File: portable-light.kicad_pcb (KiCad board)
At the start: 4 copper layers, 54.5 x 63.7 mm, 104 parts, among them J1 Prog, J2 Button, J3 Charger, J4 Seven-segment, J5 LOAD, Q1 MMBT2222A, Q2 MMBT2222A, Q3 MMBT2222A, Q4 MMBT2222A, Q5 MMBT2222A, Q6 PHD45N03LTA, Q7 PHD45N03LTA, Q8 MMBT2222A, U1 L78L05_SOT89, U2 ATmega88PA-AU, U3 LTC1733EMSEPBF, Y1 Crystal

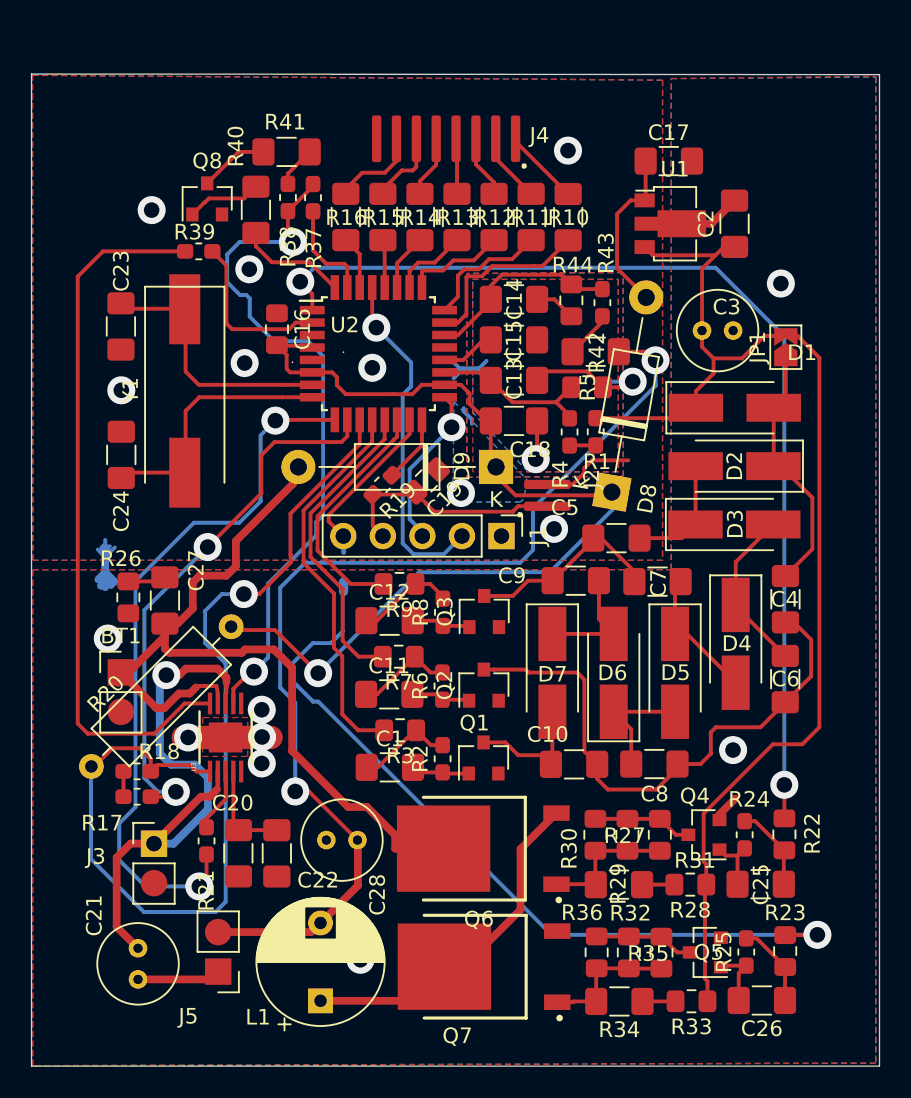
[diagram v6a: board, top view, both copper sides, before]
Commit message: divided schematics into multiple sheets moved to arch
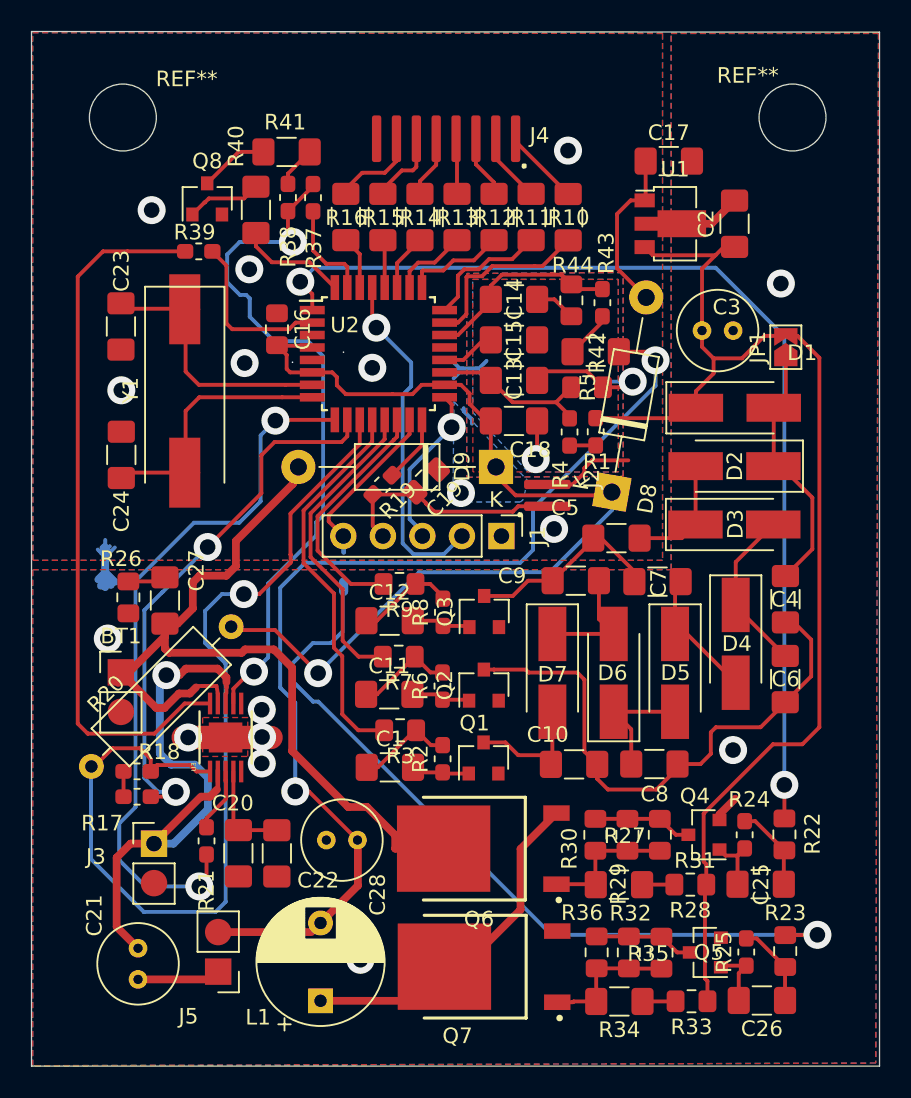
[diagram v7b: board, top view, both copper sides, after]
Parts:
- added REF**: MountingHole_4.3mm_M4, MountingHole:MountingHole_4.3mm_M4, F.Cu at (171.1, 71.0)
- added REF**: MountingHole_4.3mm_M4, MountingHole:MountingHole_4.3mm_M4, F.Cu at (128.1, 71.0)
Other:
- board size 54.5 x 63.7 mm -> 54.5 x 66.5 mm

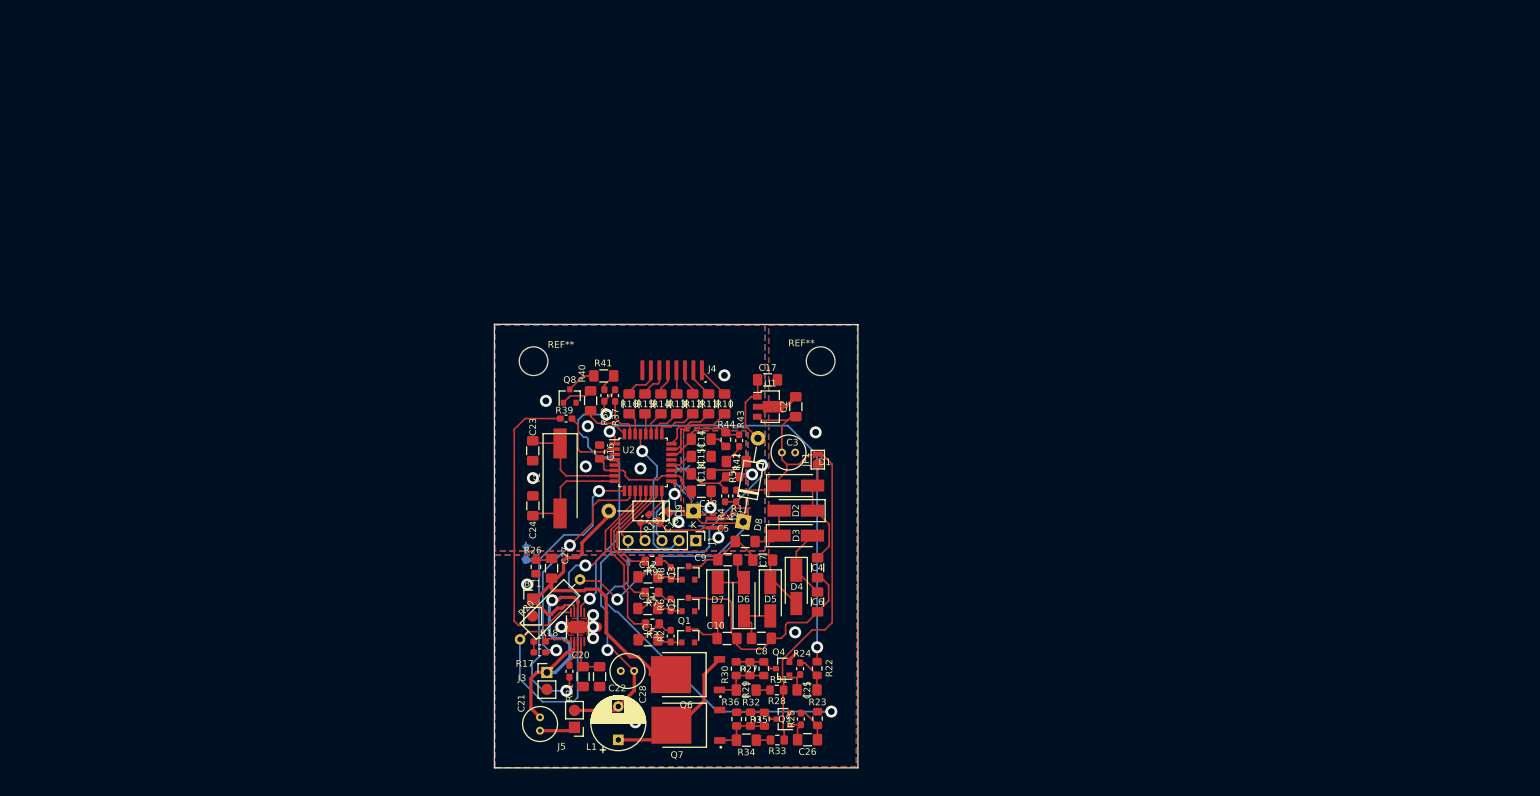
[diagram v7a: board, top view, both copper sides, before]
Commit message: Schematics redesigned and fixed
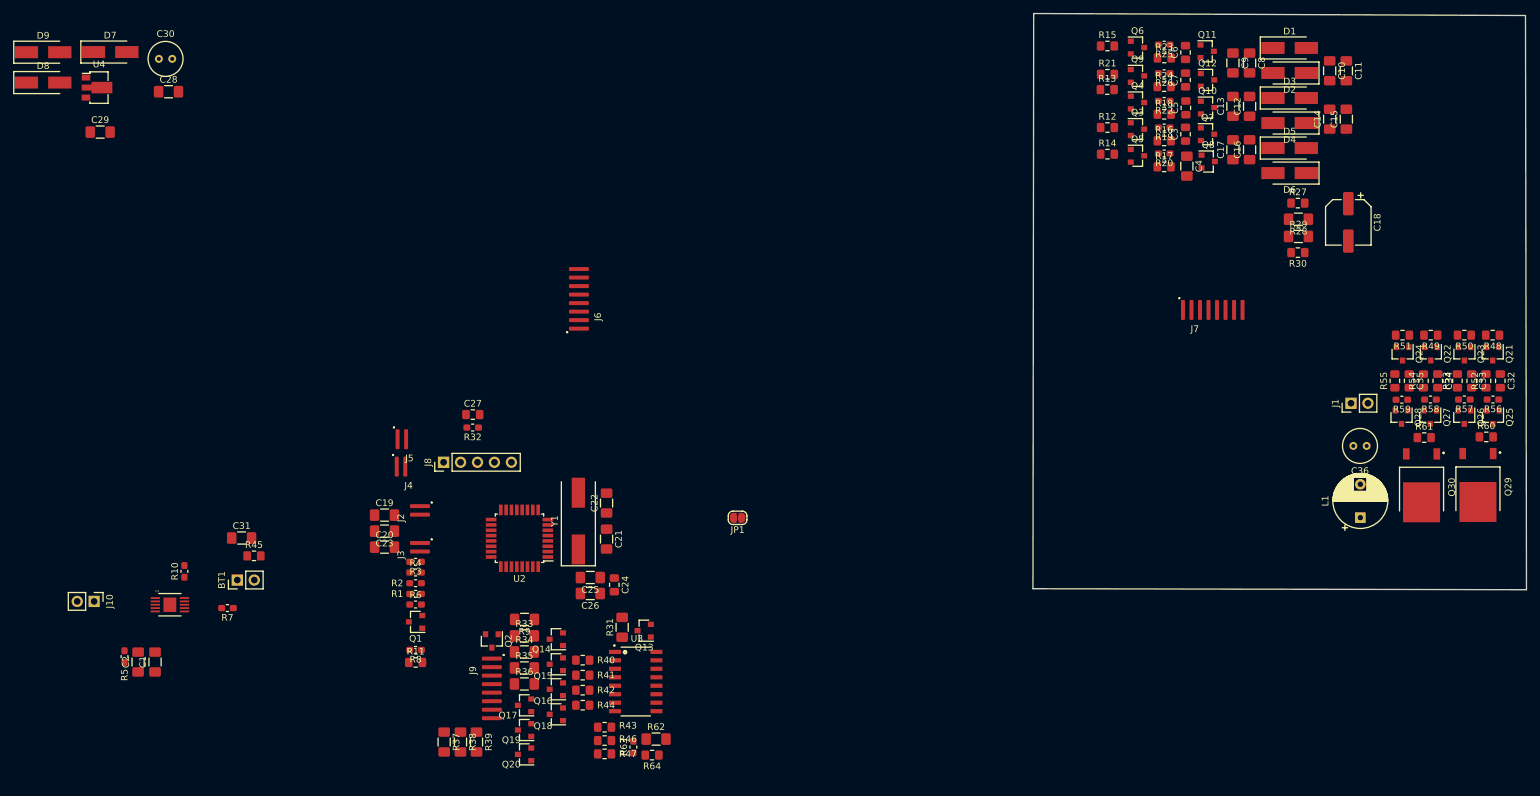
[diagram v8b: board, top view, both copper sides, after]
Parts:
- removed JP2: Jumper_2_Open, Jumper:SolderJumper-2_P1.3mm_Open_RoundedPad1.0x1.5mm
- removed NT1, NT2: Net-Tie_2, NetTie:NetTie-2_SMD_Pad0.5mm
- removed REF** (x2): MountingHole_4.3mm_M4, MountingHole:MountingHole_4.3mm_M4
- added C29: 100n, Capacitor_SMD:C_1206_3216Metric_Pad1.42x1.75mm_HandSolder, F.Cu at (63.1, 36.7)
- added C30: 10u, Capacitor_THT:C_Radial_D5.0mm_H7.0mm_P2.00mm, F.Cu at (71.9, 25.7)
- added C31: 330n, Capacitor_SMD:C_1206_3216Metric_Pad1.42x1.75mm_HandSolder, F.Cu at (84.3, 97.5)
- added C32: 10n, Capacitor_SMD:C_0805_2012Metric_Pad1.15x1.40mm_HandSolder, F.Cu at (272.9, 74.0)
- added C33: 10n, Capacitor_SMD:C_0805_2012Metric_Pad1.15x1.40mm_HandSolder, F.Cu at (268.6, 74.0)
- added C34: 10n, Capacitor_SMD:C_0805_2012Metric_Pad1.15x1.40mm_HandSolder, F.Cu at (263.6, 74.0)
- added C35: 10n, Capacitor_SMD:C_0805_2012Metric_Pad1.15x1.40mm_HandSolder, F.Cu at (259.3, 74.0)
- added C36: 10u, Capacitor_THT:C_Radial_D5.0mm_H7.0mm_P2.00mm, F.Cu at (252.9, 83.7)
- added J10: Charger, Connector_PinHeader_2.54mm:PinHeader_1x02_P2.54mm_Vertical, F.Cu at (62.2, 107.0)
- added J6: interboard-interface_2, Ribbon_Cable:Ribbon_8, F.Cu at (134.8, 66.2)
- added J7: interboard-interface_1, Ribbon_Cable:Ribbon_8, F.Cu at (225.4, 63.4)
- added J8: Conn_01x05, Connector_PinHeader_2.54mm:PinHeader_1x05_P2.54mm_Vertical, F.Cu at (114.6, 86.2)
- added J9: Conn_01x08, Ribbon_Cable:Ribbon_8, F.Cu at (121.8, 115.6)
- added Q10: S9012, Package_TO_SOT_SMD:SOT-23, F.Cu at (229.1, 33.0)
- added Q11: S9012, Package_TO_SOT_SMD:SOT-23, F.Cu at (229.0, 24.6)
- added Q12: MMBT2222, Package_TO_SOT_SMD:SOT-23, F.Cu at (229.1, 28.9)
- added Q13: Q_NMOS_DGS, Package_TO_SOT_SMD:SOT-23, F.Cu at (144.6, 111.4)
- added Q14: Q_PNP_BCE, Package_TO_SOT_SMD:SOT-23, F.Cu at (131.5, 112.7)
- added Q15: Q_PNP_BCE, Package_TO_SOT_SMD:SOT-23, F.Cu at (131.5, 116.4)
- added Q16: Q_PNP_BCE, Package_TO_SOT_SMD:SOT-23, F.Cu at (131.5, 120.2)
- added Q17: Q_PNP_BCE, Package_TO_SOT_SMD:SOT-23, F.Cu at (126.7, 122.6)
- added Q18: Q_PNP_BCE, Package_TO_SOT_SMD:SOT-23, F.Cu at (131.5, 123.9)
- added Q19: Q_PNP_BCE, Package_TO_SOT_SMD:SOT-23, F.Cu at (126.7, 126.3)
- added Q20: Q_PNP_BCE, Package_TO_SOT_SMD:SOT-23, F.Cu at (126.7, 129.9)
- added Q21: MMBT2222, Package_TO_SOT_SMD:SOT-23, F.Cu at (271.8, 69.9)
- added Q22: MMBT2222, Package_TO_SOT_SMD:SOT-23, F.Cu at (262.5, 69.9)
- added Q23: MMBT2222, Package_TO_SOT_SMD:SOT-23, F.Cu at (267.5, 69.9)
- added Q24: MMBT2222, Package_TO_SOT_SMD:SOT-23, F.Cu at (258.3, 69.9)
- added Q25: Q_PNP_BCE, Package_TO_SOT_SMD:SOT-23, F.Cu at (271.8, 79.4)
- added Q26: MMBT2222, Package_TO_SOT_SMD:SOT-23, F.Cu at (267.5, 79.4)
- added Q27: Q_PNP_BCE, Package_TO_SOT_SMD:SOT-23, F.Cu at (262.4, 79.4)
- added Q28: MMBT2222, Package_TO_SOT_SMD:SOT-23, F.Cu at (258.1, 79.4)
- added Q29: PHD45N03LTA, UniX_Generic:DPAK, F.Cu at (269.6, 89.6)
- added Q30: PHD45N03LTA, UniX_Generic:DPAK, F.Cu at (261.1, 89.6)
- added Q9: MMBT2222, Package_TO_SOT_SMD:SOT-23, F.Cu at (218.6, 28.3)
- added R45: 1R60, Resistor_SMD:R_0805_2012Metric_Pad1.15x1.40mm_HandSolder, F.Cu at (86.2, 100.2)
- added R46: 5K1, Capacitor_SMD:C_0805_2012Metric_Pad1.15x1.40mm_HandSolder, F.Cu at (138.7, 127.9)
- added R47: 5K1, Capacitor_SMD:C_0805_2012Metric_Pad1.15x1.40mm_HandSolder, F.Cu at (138.7, 129.9)
- added R48: 10K, Resistor_SMD:R_0805_2012Metric_Pad1.15x1.40mm_HandSolder, F.Cu at (271.8, 67.1)
- added R49: 10K, Resistor_SMD:R_0805_2012Metric_Pad1.15x1.40mm_HandSolder, F.Cu at (262.5, 67.1)
- added R50: 10K, Resistor_SMD:R_0805_2012Metric_Pad1.15x1.40mm_HandSolder, F.Cu at (267.5, 67.1)
- added R51: 10K, Resistor_SMD:R_0805_2012Metric_Pad1.15x1.40mm_HandSolder, F.Cu at (258.3, 67.1)
- added R52: 56R, Resistor_SMD:R_0805_2012Metric_Pad1.15x1.40mm_HandSolder, F.Cu at (270.8, 74.0)
- added R53: 56R, Resistor_SMD:R_0805_2012Metric_Pad1.15x1.40mm_HandSolder, F.Cu at (266.5, 74.0)
- added R54: 56R, Resistor_SMD:R_0805_2012Metric_Pad1.15x1.40mm_HandSolder, F.Cu at (261.4, 74.0)
- added R55: 56R, Resistor_SMD:R_0805_2012Metric_Pad1.15x1.40mm_HandSolder, F.Cu at (257.1, 74.0)
- added R56: 1K, Resistor_SMD:R_0603_1608Metric_Pad1.05x0.95mm_HandSolder, F.Cu at (271.8, 76.8)
- added R57: 1K, Resistor_SMD:R_0603_1608Metric_Pad1.05x0.95mm_HandSolder, F.Cu at (267.5, 76.8)
- added R58: 1K, Resistor_SMD:R_0603_1608Metric_Pad1.05x0.95mm_HandSolder, F.Cu at (262.5, 76.8)
- added R59: 1K, Resistor_SMD:R_0603_1608Metric_Pad1.05x0.95mm_HandSolder, F.Cu at (258.2, 76.8)
- added R60: 33R, Resistor_SMD:R_0805_2012Metric_Pad1.15x1.40mm_HandSolder, F.Cu at (270.8, 82.4)
- added R61: 33R, Resistor_SMD:R_0805_2012Metric_Pad1.15x1.40mm_HandSolder, F.Cu at (261.5, 82.5)
- added R62: 475R, Resistor_SMD:R_1206_3216Metric_Pad1.42x1.75mm_HandSolder, F.Cu at (146.4, 127.7)
- added R63: 1K, Resistor_SMD:R_0603_1608Metric_Pad1.05x0.95mm_HandSolder, F.Cu at (143.0, 128.9)
- added R64: 475R, Resistor_SMD:R_0805_2012Metric_Pad1.15x1.40mm_HandSolder, F.Cu at (145.8, 130.1)
- added U4: L78L05_SOT89, Package_TO_SOT_SMD:SOT-89-3, F.Cu at (62.6, 30.0)
- C1, C25, C26: value 10n -> 100n
- C10, C15, C17, C8, C9: value 100n -> 330n
- C11, C12: value 10n -> 330n
- C13, C14: value 15n -> 330n
- C16: value 300n -> 330n; footprint Capacitor_SMD:C_0805_2012Metric_Pad1.15x1.40mm_HandSolder -> Capacitor_SMD:C_1206_3216Metric_Pad1.42x1.75mm_HandSolder
- C18: value 100n -> 100u; footprint Capacitor_SMD:C_1206_3216Metric_Pad1.42x1.75mm_HandSolder -> Capacitor_SMD:CP_Elec_6.3x5.9
- C19: value 300n -> 15n; footprint Capacitor_SMD:C_0805_2012Metric_Pad1.15x1.40mm_HandSolder -> Capacitor_SMD:C_1206_3216Metric_Pad1.42x1.75mm_HandSolder
- C20: value 100n -> 15n
- C21: value 10u -> 22p; footprint Capacitor_THT:C_Radial_D5.0mm_H7.0mm_P2.00mm -> Capacitor_SMD:C_1206_3216Metric_Pad1.42x1.75mm_HandSolder
- C22: value 100n -> 22p
- C23: value 22p -> 100n
- C24: value 22p -> 300n; footprint Capacitor_SMD:C_1206_3216Metric_Pad1.42x1.75mm_HandSolder -> Capacitor_SMD:C_0805_2012Metric_Pad1.15x1.40mm_HandSolder
- C27: value 330n -> 300n; footprint Capacitor_SMD:C_1206_3216Metric_Pad1.42x1.75mm_HandSolder -> Capacitor_SMD:C_0805_2012Metric_Pad1.15x1.40mm_HandSolder
- C28: value 10u -> 100n; footprint Capacitor_THT:C_Radial_D5.0mm_H7.0mm_P2.00mm -> Capacitor_SMD:C_1206_3216Metric_Pad1.42x1.75mm_HandSolder
- C3: value 10u -> 10n; footprint Capacitor_THT:C_Radial_D5.0mm_H7.0mm_P2.00mm -> Capacitor_SMD:C_0805_2012Metric_Pad1.15x1.40mm_HandSolder
- C4: value 100n -> 10n-big
- C5, C6, C7: value 100n -> 10n; footprint Capacitor_SMD:C_1206_3216Metric_Pad1.42x1.75mm_HandSolder -> Capacitor_SMD:C_0805_2012Metric_Pad1.15x1.40mm_HandSolder
- D7: value 1N5819 -> M7
- D8, D9: footprint Diode_THT:D_DO-41_SOD81_P12.70mm_Horizontal -> Diode_SMD:D_SMA_Handsoldering
- J1: value Prog -> LOAD; footprint Connector_PinHeader_2.54mm:PinHeader_1x05_P2.54mm_Vertical -> Connector_PinHeader_2.54mm:PinHeader_1x02_P2.54mm_Vertical
- J2: value Button -> conn_sense_pump_2
- J3: value Charger -> conn_sense_buck_2; footprint Connector_PinHeader_2.54mm:PinHeader_1x02_P2.54mm_Vertical -> Ribbon_Cable:Ribbon_2
- J4: value Seven-segment -> conn_sense_pump_1; footprint Ribbon_Cable:Ribbon_8 -> Ribbon_Cable:Ribbon_2
- J5: value LOAD -> conn_sense_buck_1; footprint Connector_PinHeader_2.54mm:PinHeader_1x02_P2.54mm_Vertical -> Ribbon_Cable:Ribbon_2
- JP1: value SolderJumper_2_Open -> Jumper_Mosfet_Open; footprint Jumper:SolderJumper-2_P1.3mm_Open_TrianglePad1.0x1.5mm -> Jumper:SolderJumper-2_P1.3mm_Open_RoundedPad1.0x1.5mm
- Q1: value MMBT2222A -> Q_PNP_BCE
- Q3, Q4, Q5, Q8: value MMBT2222A -> MMBT2222
- Q6: value PHD45N03LTA -> MMBT2222; footprint UniX_Generic:DPAK -> Package_TO_SOT_SMD:SOT-23
- Q7: value PHD45N03LTA -> S9012; footprint UniX_Generic:DPAK -> Package_TO_SOT_SMD:SOT-23
- R1: value 1k -> 1K
- R10: value 475R -> 1K; footprint Resistor_SMD:R_1206_3216Metric_Pad1.42x1.75mm_HandSolder -> Resistor_SMD:R_0603_1608Metric_Pad1.05x0.95mm_HandSolder
- R11: value 475R -> 510R; footprint Resistor_SMD:R_1206_3216Metric_Pad1.42x1.75mm_HandSolder -> Resistor_SMD:R_0805_2012Metric_Pad1.15x1.40mm_HandSolder
- R12, R13, R14, R15: value 475R -> 10K; footprint Resistor_SMD:R_1206_3216Metric_Pad1.42x1.75mm_HandSolder -> Capacitor_SMD:C_0805_2012Metric_Pad1.15x1.40mm_HandSolder
- R16: value 475R -> 56R; footprint Resistor_SMD:R_1206_3216Metric_Pad1.42x1.75mm_HandSolder -> Capacitor_SMD:C_0805_2012Metric_Pad1.15x1.40mm_HandSolder
- R17, R18, R24: value 1K -> 56R; footprint Resistor_SMD:R_0603_1608Metric_Pad1.05x0.95mm_HandSolder -> Capacitor_SMD:C_0805_2012Metric_Pad1.15x1.40mm_HandSolder
- R20: value 500K -> 1K; footprint Resistor_THT:R_Axial_DIN0309_L9.0mm_D3.2mm_P12.70mm_Horizontal -> Resistor_SMD:R_0603_1608Metric_Pad1.05x0.95mm_HandSolder
- R21: value 1K -> 10K; footprint Resistor_SMD:R_0603_1608Metric_Pad1.05x0.95mm_HandSolder -> Capacitor_SMD:C_0805_2012Metric_Pad1.15x1.40mm_HandSolder
- R22, R7: value 33R -> 1K; footprint Resistor_SMD:R_0805_2012Metric_Pad1.15x1.40mm_HandSolder -> Resistor_SMD:R_0603_1608Metric_Pad1.05x0.95mm_HandSolder
- R23: value 33R -> 56R; footprint Resistor_SMD:R_0805_2012Metric_Pad1.15x1.40mm_HandSolder -> Capacitor_SMD:C_0805_2012Metric_Pad1.15x1.40mm_HandSolder
- R26: value 1R60 -> 1K; footprint Resistor_SMD:R_0805_2012Metric_Pad1.15x1.40mm_HandSolder -> Resistor_SMD:R_0603_1608Metric_Pad1.05x0.95mm_HandSolder
- R27: value 56R -> 10K; footprint Resistor_SMD:R_0805_2012Metric_Pad1.15x1.40mm_HandSolder -> Capacitor_SMD:C_0805_2012Metric_Pad1.15x1.40mm_HandSolder
- R28: value 56R -> 475R; footprint Resistor_SMD:R_0805_2012Metric_Pad1.15x1.40mm_HandSolder -> Capacitor_SMD:C_1206_3216Metric_Pad1.42x1.75mm_HandSolder
- R29: value 100R -> 140R; footprint Resistor_SMD:R_1206_3216Metric_Pad1.42x1.75mm_HandSolder -> Capacitor_SMD:C_1206_3216Metric_Pad1.42x1.75mm_HandSolder
- R3: value 33R -> 150K; footprint Resistor_SMD:R_0805_2012Metric_Pad1.15x1.40mm_HandSolder -> Resistor_SMD:R_0603_1608Metric_Pad1.05x0.95mm_HandSolder
- R30: footprint Resistor_SMD:R_0805_2012Metric_Pad1.15x1.40mm_HandSolder -> Capacitor_SMD:C_0805_2012Metric_Pad1.15x1.40mm_HandSolder
- R31: value 56R -> 10K; footprint Resistor_SMD:R_0805_2012Metric_Pad1.15x1.40mm_HandSolder -> Resistor_SMD:R_1206_3216Metric_Pad1.42x1.75mm_HandSolder
- R32, R5: value 56R -> 1K; footprint Resistor_SMD:R_0805_2012Metric_Pad1.15x1.40mm_HandSolder -> Resistor_SMD:R_0603_1608Metric_Pad1.05x0.95mm_HandSolder
- R33, R35, R36: value 56R -> 475R; footprint Resistor_SMD:R_0805_2012Metric_Pad1.15x1.40mm_HandSolder -> Resistor_SMD:R_1206_3216Metric_Pad1.42x1.75mm_HandSolder
- R34: value 100R -> 475R
- R37, R38, R39: value 1K -> 475R; footprint Resistor_SMD:R_0603_1608Metric_Pad1.05x0.95mm_HandSolder -> Resistor_SMD:R_1206_3216Metric_Pad1.42x1.75mm_HandSolder
- R4: value 1k -> 270K
- R40: value 10K -> 5K1; footprint Resistor_SMD:R_1206_3216Metric_Pad1.42x1.75mm_HandSolder -> Capacitor_SMD:C_0805_2012Metric_Pad1.15x1.40mm_HandSolder
- R41, R42: value 475R -> 5K1; footprint Resistor_SMD:R_1206_3216Metric_Pad1.42x1.75mm_HandSolder -> Capacitor_SMD:C_0805_2012Metric_Pad1.15x1.40mm_HandSolder
- R43: value 1K -> 5K1; footprint Resistor_SMD:R_0603_1608Metric_Pad1.05x0.95mm_HandSolder -> Capacitor_SMD:C_0805_2012Metric_Pad1.15x1.40mm_HandSolder
- R44: value 475R -> 5K1; footprint Resistor_SMD:R_0805_2012Metric_Pad1.15x1.40mm_HandSolder -> Capacitor_SMD:C_0805_2012Metric_Pad1.15x1.40mm_HandSolder
- R6: value 1K -> 10K
- R9: value 33R -> 10K; footprint Resistor_SMD:R_0805_2012Metric_Pad1.15x1.40mm_HandSolder -> Resistor_SMD:R_1206_3216Metric_Pad1.42x1.75mm_HandSolder
- U1: value L78L05_SOT89 -> LTC1733EMSEPBF; footprint Package_TO_SOT_SMD:SOT-89-3 -> UniX_Generic:MSOP-10_MSE
- U3: value LTC1733EMSEPBF -> CD4094BPW; footprint UniX_Generic:MSOP-10_MSE -> UniX_Generic:SOP-16
- Y1: value Crystal -> 20MHz Crystal
- moved C11 132.1 mm to (249.9, 27.5), turned to 270 degrees
- moved C10 124.1 mm to (247.4, 27.5), turned to 270 degrees
- moved D8 123.9 mm to (54.6, 29.3), turned to 0 degrees
- moved D7 122.5 mm to (64.6, 24.7), turned to 0 degrees
- moved R18 122.5 mm to (222.6, 34.0)
- moved R20 120.9 mm to (222.6, 39.9), turned to 180 degrees
- moved R21 120.4 mm to (214.1, 28.0), turned to 0 degrees
- moved R26 119.7 mm to (222.6, 27.9), turned to 180 degrees
- moved D9 119.3 mm to (54.6, 24.7), turned to 0 degrees
- moved R17 118.5 mm to (222.6, 41.9), turned to 0 degrees
- moved Q7 117.9 mm to (229.1, 37.0), turned to 0 degrees
- moved L1 116.1 mm to (251.9, 94.5)
- moved Q6 115.6 mm to (218.6, 24.0), turned to 0 degrees
- moved R25 114.8 mm to (222.6, 23.6), turned to 180 degrees
- moved C12 114.5 mm to (235.4, 32.8), turned to 90 degrees
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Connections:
- C1 pad 2: Net-(C1-Pad2) -> GNDPWR
- C11 pad 1: Net-(C11-Pad1) -> Net-(C10-Pad1)
- C11 pad 2: Net-(C11-Pad2) -> Net-(C10-Pad2)
- C13 pad 1: GNDA -> Net-(C12-Pad1)
- C13 pad 2: /sense_pump -> Net-(C12-Pad2)
- C14 pad 1: GNDA -> Net-(C14-Pad1)
- C14 pad 2: /sense_led -> Net-(C10-Pad2)
- C15 pad 1: Net-(C15-Pad1) -> Net-(C14-Pad1)
- C15 pad 2: GNDA -> Net-(C10-Pad2)
- C16 pad 1: GND -> Net-(C16-Pad1)
- C16 pad 2: VBUS -> Net-(C12-Pad2)
- C17 pad 1: Net-(C17-Pad1) -> Net-(C16-Pad1)
- C17 pad 2: GNDPWR -> Net-(C12-Pad2)
- C18 pad 1: GNDA -> +8V
- C18 pad 2: VBUS -> GNDPWR
- C19 pad 2: /miso-and-button -> /vsense_pump_2
- C2 pad 1: +15V -> Net-(C1-Pad1)
- C20 pad 1: Net-(C20-Pad1) -> GND
- C20 pad 2: GNDPWR -> /vsense_buck_2
- C21 pad 1: VDC -> GND
- C21 pad 2: GNDPWR -> /Controller/xtal1
- C22 pad 1: Net-(C20-Pad1) -> GND
- C22 pad 2: GNDPWR -> /Controller/xtal2
- C23 pad 1: GND -> Net-(C23-Pad1)
- C23 pad 2: Net-(C23-Pad2) -> GND
- C24 pad 2: Net-(C24-Pad2) -> VBUS
- C25 pad 1: Net-(C25-Pad1) -> GND
- C25 pad 2: Net-(C25-Pad2) -> VBUS
- C26 pad 1: Net-(C26-Pad1) -> GND
- C26 pad 2: Net-(C26-Pad2) -> VBUS
- C27 pad 1: +BATT -> GND
- C27 pad 2: Net-(C27-Pad2) -> /Controller/button
- C28 pad 1: Net-(C28-Pad1) -> +8V
- C3 pad 1: +15V -> Net-(C3-Pad1)
- C3 pad 2: GNDPWR -> Net-(C3-Pad2)
- C4 pad 2: Net-(C10-Pad2) -> Net-(C4-Pad2)
- C6 pad 2: Net-(C10-Pad2) -> Net-(C6-Pad2)
- C7 pad 2: Net-(C5-Pad2) -> Net-(C7-Pad2)
- C8 pad 2: Net-(C10-Pad2) -> Net-(C12-Pad2)
- C9 pad 1: Net-(C9-Pad1) -> Net-(C8-Pad1)
- C9 pad 2: Net-(C5-Pad2) -> Net-(C12-Pad2)
- D1 pad 1: +15V -> Net-(C8-Pad1)
- D1 pad 2: Net-(C4-Pad1) -> Net-(D1-Pad2)
- D2 pad 1: Net-(C4-Pad1) -> Net-(C10-Pad1)
- D2 pad 2: Net-(C5-Pad1) -> Net-(C8-Pad1)
- D3 pad 1: Net-(C5-Pad1) -> Net-(C12-Pad1)
- D3 pad 2: Net-(C6-Pad1) -> Net-(C10-Pad1)
- D4 pad 1: Net-(C6-Pad1) -> Net-(C14-Pad1)
- D4 pad 2: Net-(C7-Pad1) -> Net-(C12-Pad1)
- D5 pad 1: Net-(C7-Pad1) -> Net-(C16-Pad1)
- D5 pad 2: Net-(C8-Pad1) -> Net-(C14-Pad1)
- D6 pad 1: Net-(C8-Pad1) -> +8V
- D6 pad 2: Net-(C9-Pad1) -> Net-(C16-Pad1)
- D7 pad 1: Net-(C9-Pad1) -> +8V
- D7 pad 2: Net-(C10-Pad1) -> Net-(C29-Pad1)
- D8 pad 2: Net-(C17-Pad1) -> Net-(C29-Pad1)
- J1 pad 1: GND -> GNDPWR
- J1 pad 2: /reset -> /Buck converter/vout
- J2 pad 1: /miso-and-button -> GNDA
- J2 pad 2: GND -> /vsense_pump_2
- J3 pad 1: VDC -> GNDA
- J3 pad 2: GNDPWR -> /vsense_buck_2
- J4 pad 1: Net-(J4-Pad1) -> GNDA
- J4 pad 2: Net-(J4-Pad2) -> (no net)
- J5 pad 1: GNDPWR -> GNDA
- J5 pad 2: Net-(C28-Pad1) -> (no net)
- JP1 pad 1: Net-(C4-Pad1) -> /Controller/mosi
- JP1 pad 2: +15V -> /buck_high_mos_low_bjt_2
- L1 pad 2: Net-(C28-Pad1) -> /Buck converter/vout
- Q1 pad 1: Net-(C1-Pad2) -> Net-(Q1-Pad1)
- Q1 pad 2: GNDPWR -> +BATT
- Q1 pad 3: Net-(C10-Pad1) -> Net-(Q1-Pad3)
- Q2 pad 1: Net-(C11-Pad2) -> Net-(Q2-Pad1)
- Q2 pad 2: GNDPWR -> GND
- Q2 pad 3: Net-(C10-Pad2) -> Net-(Q2-Pad3)
- Q3 pad 1: Net-(C12-Pad2) -> Net-(Q3-Pad1)
- Q3 pad 3: Net-(C5-Pad2) -> Net-(Q3-Pad3)
- Q4 pad 1: Net-(C25-Pad2) -> Net-(Q4-Pad1)
- Q5 pad 1: Net-(C26-Pad2) -> Net-(Q5-Pad1)
- Q6 pad 3: Net-(L1-Pad1) -> Net-(Q6-Pad3)
- Q7 pad 1: Net-(Q7-Pad1) -> Net-(C3-Pad2)
- Q7 pad 3: GNDPWR -> Net-(C12-Pad2)
- Q8 pad 1: Net-(Q8-Pad1) -> Net-(C4-Pad1)
- Q8 pad 2: GND -> GNDPWR
- Q8 pad 3: Net-(Q8-Pad3) -> Net-(C12-Pad2)
- R1 pad 1: Net-(R1-Pad1) -> /Controller/charger_chrg_pulldown_or_float_out
- R1 pad 2: +15V -> Net-(R1-Pad2)
- R10 pad 1: Net-(J4-Pad1) -> Net-(R10-Pad1)
- R10 pad 2: Net-(R10-Pad2) -> /Charger/acpr_out
- R11 pad 1: Net-(J4-Pad2) -> Net-(R11-Pad1)
- R11 pad 2: Net-(R11-Pad2) -> Net-(Q2-Pad3)
- R12 pad 1: Net-(J4-Pad3) -> /pump_clka_1
- R12 pad 2: Net-(R12-Pad2) -> Net-(Q3-Pad1)
- R13 pad 1: Net-(J4-Pad4) -> /pump_onoff_1
- R13 pad 2: Net-(R13-Pad2) -> Net-(Q4-Pad1)
- R14 pad 1: Net-(J4-Pad5) -> /pump_clkb_1
- R14 pad 2: Net-(R14-Pad2) -> Net-(Q5-Pad1)
- R15 pad 1: Net-(J4-Pad6) -> /pump_clkb_1
- R15 pad 2: Net-(R15-Pad2) -> Net-(Q6-Pad1)
- R16 pad 1: Net-(J4-Pad7) -> Net-(Q3-Pad3)
- R16 pad 2: Net-(R16-Pad2) -> Net-(C3-Pad1)
- R17 pad 1: /chrg_out -> Net-(Q5-Pad3)
- R17 pad 2: Net-(R17-Pad2) -> Net-(C4-Pad2)
- R18 pad 1: Net-(R17-Pad2) -> Net-(Q4-Pad3)
- R18 pad 2: /chrg_in -> Net-(C5-Pad1)
- R19 pad 1: Net-(R19-Pad1) -> Net-(C3-Pad2)
- R19 pad 2: /miso-and-button -> Net-(C3-Pad1)
- R2 pad 1: Net-(C1-Pad2) -> Net-(R1-Pad2)
- R2 pad 2: Net-(C1-Pad1) -> /Controller/charger_chrg_in
- R20 pad 1: /chrg_in -> Net-(C4-Pad1)
- R20 pad 2: VBUS -> Net-(C4-Pad2)
- R21 pad 1: /fault_in -> /pump_clka_1
- R21 pad 2: Net-(R21-Pad2) -> Net-(Q9-Pad1)
- R22 pad 1: Net-(C25-Pad1) -> Net-(C5-Pad2)
- R22 pad 2: /high_mos_oc2a -> Net-(C5-Pad1)
- R23 pad 1: Net-(C26-Pad1) -> Net-(Q6-Pad3)
- R23 pad 2: /low_mos_oc2b -> Net-(C6-Pad1)
- R24 pad 1: Net-(C25-Pad2) -> Net-(Q9-Pad3)
- R24 pad 2: Net-(C25-Pad1) -> Net-(C7-Pad1)
- R25 pad 1: Net-(C26-Pad2) -> Net-(C6-Pad2)
- R25 pad 2: Net-(C26-Pad1) -> Net-(C6-Pad1)
- R26 pad 1: Net-(C27-Pad2) -> Net-(C7-Pad2)
- R26 pad 2: GNDPWR -> Net-(C7-Pad1)
- R27 pad 1: Net-(Q4-Pad3) -> +8V
- R27 pad 2: Net-(Q6-Pad1) -> /vsense_pump
- R28 pad 1: +15V -> /vsense_pump
- R29 pad 2: Net-(Q6-Pad1) -> Net-(R29-Pad2)
- R3 pad 1: Net-(C1-Pad1) -> VBUS
- R3 pad 2: /pump-in -> Net-(R3-Pad2)
- R30 pad 1: Net-(Q4-Pad3) -> Net-(R29-Pad2)
- R30 pad 2: Net-(Q6-Pad1) -> GND
- R31 pad 1: Net-(Q4-Pad3) -> Net-(Q13-Pad2)
- R31 pad 2: Net-(Q6-Pad1) -> /Controller/shiftregister-vss
- R32 pad 1: Net-(Q5-Pad3) -> /Controller/miso
- R32 pad 2: Net-(Q7-Pad1) -> /Controller/button
- R33 pad 1: +15V -> Net-(J9-Pad1)
- R33 pad 2: Net-(R33-Pad2) -> /Controller/seg-1
- R34 pad 1: Net-(R33-Pad2) -> Net-(J9-Pad2)
- R34 pad 2: Net-(Q7-Pad1) -> /Controller/seg-2
- R35 pad 1: Net-(Q5-Pad3) -> Net-(J9-Pad3)
- R35 pad 2: Net-(Q7-Pad1) -> /Controller/seg-3
- R36 pad 1: Net-(Q5-Pad3) -> Net-(J9-Pad4)
- R36 pad 2: Net-(Q7-Pad1) -> /Controller/seg-4
- R37 pad 1: Net-(R37-Pad1) -> Net-(J9-Pad5)
- R37 pad 2: /prog_pullup -> /Controller/seg-5
- R38 pad 1: Net-(R37-Pad1) -> Net-(J9-Pad6)
- R38 pad 2: Net-(R38-Pad2) -> /Controller/seg-6
- R39 pad 1: Net-(R39-Pad1) -> Net-(J9-Pad7)
- R39 pad 2: /acpr_in -> /Controller/seg-7
- R4 pad 1: /sense_pump -> Net-(R3-Pad2)
- R4 pad 2: Net-(R1-Pad1) -> /Controller/charger_chrg_in
- R40 pad 1: /prog_pulldown -> Net-(Q14-Pad1)
- R40 pad 2: Net-(Q8-Pad1) -> /Controller/seg-base-1
- R41 pad 1: Net-(R38-Pad2) -> Net-(Q15-Pad1)
- R41 pad 2: Net-(Q8-Pad3) -> /Controller/seg-base-2
- R42 pad 1: Net-(R42-Pad1) -> Net-(Q16-Pad1)
- R42 pad 2: Net-(C28-Pad1) -> /Controller/seg-base-3
- R43 pad 1: /sense_led -> Net-(Q17-Pad1)
- R43 pad 2: Net-(R42-Pad1) -> /Controller/seg-base-5
- R44 pad 1: GNDA -> Net-(Q18-Pad1)
- R44 pad 2: /sense_led -> /Controller/seg-base-4
- R5 pad 1: GNDA -> /Controller/charger_fault_in
- R5 pad 2: /sense_pump -> Net-(R5-Pad2)
- R6 pad 1: Net-(C11-Pad2) -> Net-(Q1-Pad1)
- R6 pad 2: Net-(C11-Pad1) -> /Controller/charger_prog_enable_charging
- R7 pad 1: Net-(C11-Pad1) -> Net-(Q1-Pad3)
- R7 pad 2: /pump-clka_oc1a -> Net-(R7-Pad2)
- R8 pad 1: Net-(C12-Pad2) -> Net-(R7-Pad2)
- R8 pad 2: Net-(C12-Pad1) -> Net-(R11-Pad1)
- R9 pad 1: Net-(C12-Pad1) -> /Controller/charger_prog_disable_charging
- R9 pad 2: /pump-clkb_oc1b -> Net-(Q2-Pad1)
- U1 pad 1: Net-(C17-Pad1) -> /Controller/charger_chrg_in
- U1 pad 2: GNDPWR -> VDC
- U1 pad 3: +15V -> Net-(R5-Pad2)
- U2 pad 1: /high_mos_oc2a -> /buck_high_mos_high_bjt_2
- U2 pad 10: /chrg_out -> /buck_low_mos_low_bjt_2
- U2 pad 11: /chrg_in -> /Controller/shiftregister-vss
- U2 pad 12: /pump-in -> /pump_onoff_2
- U2 pad 13: /pump-clka_oc1a -> /pump_clka_2
- U2 pad 14: /pump-clkb_oc1b -> /pump_clkb_2
- U2 pad 15: /mosi -> /Controller/mosi
- U2 pad 16: Net-(R19-Pad1) -> /Controller/miso
- U2 pad 17: /sck -> /Controller/sck
- U2 pad 19: /sense_pump -> /vsense_pump_2
- U2 pad 2: /acpr_in -> /Controller/shiftregister-enable
- U2 pad 20: Net-(C15-Pad1) -> Net-(C23-Pad1)
- U2 pad 22: /sense_led -> /vsense_buck_2
- U2 pad 23: Net-(R10-Pad2) -> /Controller/charger_chrg_in
- U2 pad 24: Net-(R11-Pad2) -> /Controller/charger_fault_in
- U2 pad 25: Net-(R12-Pad2) -> /Charger/acpr_out
- U2 pad 26: Net-(R13-Pad2) -> /Controller/charger_chrg_pulldown_or_float_out
- U2 pad 27: Net-(R14-Pad2) -> /Controller/charger_prog_enable_charging
- U2 pad 28: Net-(R15-Pad2) -> /Controller/charger_prog_disable_charging
- U2 pad 29: /reset -> /Controller/reset
- U2 pad 30: Net-(R16-Pad2) -> /Controller/shiftregister-clock
- U2 pad 31: /prog_pullup -> /Controller/shiftregister-data
- U2 pad 32: /prog_pulldown -> /Controller/shiftregister-strobe
- U2 pad 7: Net-(C23-Pad2) -> /Controller/xtal1
- U2 pad 8: Net-(C24-Pad2) -> /Controller/xtal2
- U2 pad 9: /fault_in -> /buck_low_mos_high_bjt_2
- U3 pad 1: /chrg_in -> /Controller/shiftregister-strobe
- U3 pad 10: Net-(R39-Pad1) -> (no net)
- U3 pad 11: GNDPWR -> (no net)
- U3 pad 2: VDC -> /Controller/shiftregister-data
- U3 pad 3: Net-(R21-Pad2) -> /Controller/shiftregister-clock
- U3 pad 4: Net-(C20-Pad1) -> /Controller/seg-base-1
- U3 pad 5: GNDPWR -> /Controller/seg-base-2
- U3 pad 6: GNDPWR -> /Controller/seg-base-3
- U3 pad 7: Net-(R37-Pad1) -> /Controller/seg-base-4
- U3 pad 8: VDC -> Net-(Q13-Pad1)
- U3 pad 9: +BATT -> (no net)
- Y1 pad 1: Net-(C23-Pad2) -> /Controller/xtal1
- Y1 pad 2: Net-(C24-Pad2) -> /Controller/xtal2
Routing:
- net +15V: track 77.5 -> 0.00 mm
- net Net-(C28-Pad1): track 67.2 -> 0.00 mm, vias 2 -> 0
- net /high_mos_oc2a: track 66.0 -> 0.00 mm, vias 2 -> 0
- net VBUS: track 62.8 -> 0.00 mm, vias 1 -> 0
- net /chrg_in: track 62.8 -> 0.00 mm, vias 1 -> 0
- net +BATT: track 56.9 -> 0.00 mm
- net /low_mos_oc2b: track 51.4 -> 0.00 mm, vias 1 -> 0
- net /fault_in: track 46.4 -> 0.00 mm, vias 2 -> 0
- net Net-(R39-Pad1): track 45.9 -> 0.00 mm
- net Net-(R37-Pad1): track 44.7 -> 0.00 mm, vias 2 -> 0
- net VDC: track 36.9 -> 0.00 mm, vias 1 -> 0
- net Net-(C10-Pad2): track 35.9 -> 0.00 mm
- net /chrg_out: track 35.1 -> 0.00 mm, vias 2 -> 0
- net /pump-in: track 24.9 -> 0.00 mm
- net GNDPWR: track 23.8 -> 0.00 mm, vias 8 -> 0
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- removed copper zone on B.Cu, net GND
- removed copper zone on F.Cu, net GND
- removed copper zone on B.Cu, net GNDA
- removed copper zone on F.Cu, net GNDA
- removed copper zone on B.Cu, net GNDPWR
- removed copper zone on F.Cu, net GNDPWR
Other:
- board size 54.5 x 66.5 mm -> 74 x 86.4 mm
- copper layers 4 -> 10
- rule via_min_drill: 0.3 -> 0.0001
- rule via_min_size: 0.4 -> 0.001
